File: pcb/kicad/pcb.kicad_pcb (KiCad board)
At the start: 2 copper layers, 56.3 x 62.8 mm, 45 parts, among them J1 Raspberry_Pi_2_3, U1 MCP4822, U2 TL082, U3 TL082, U4 LM358, U5 ADC0831, U6 AOZ1282CI

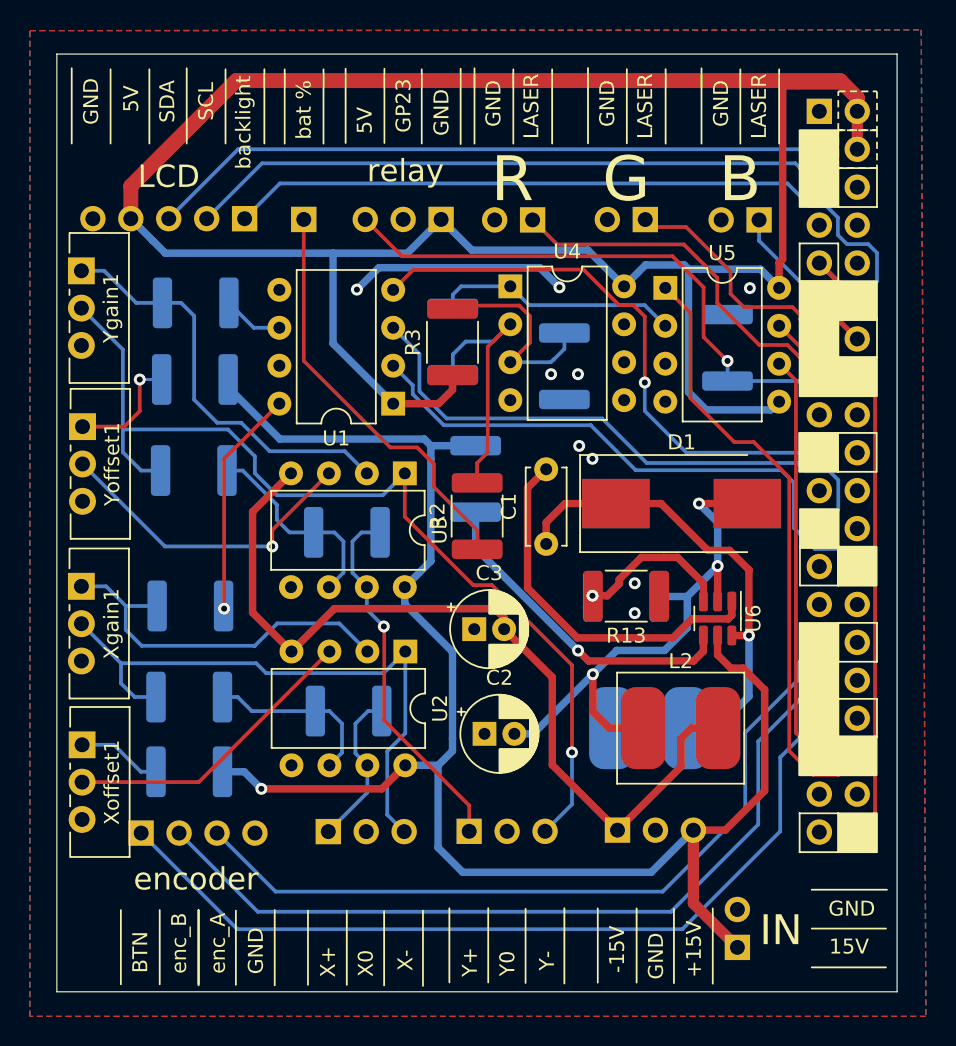
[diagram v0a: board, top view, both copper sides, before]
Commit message: jlc order sent - pcb finished
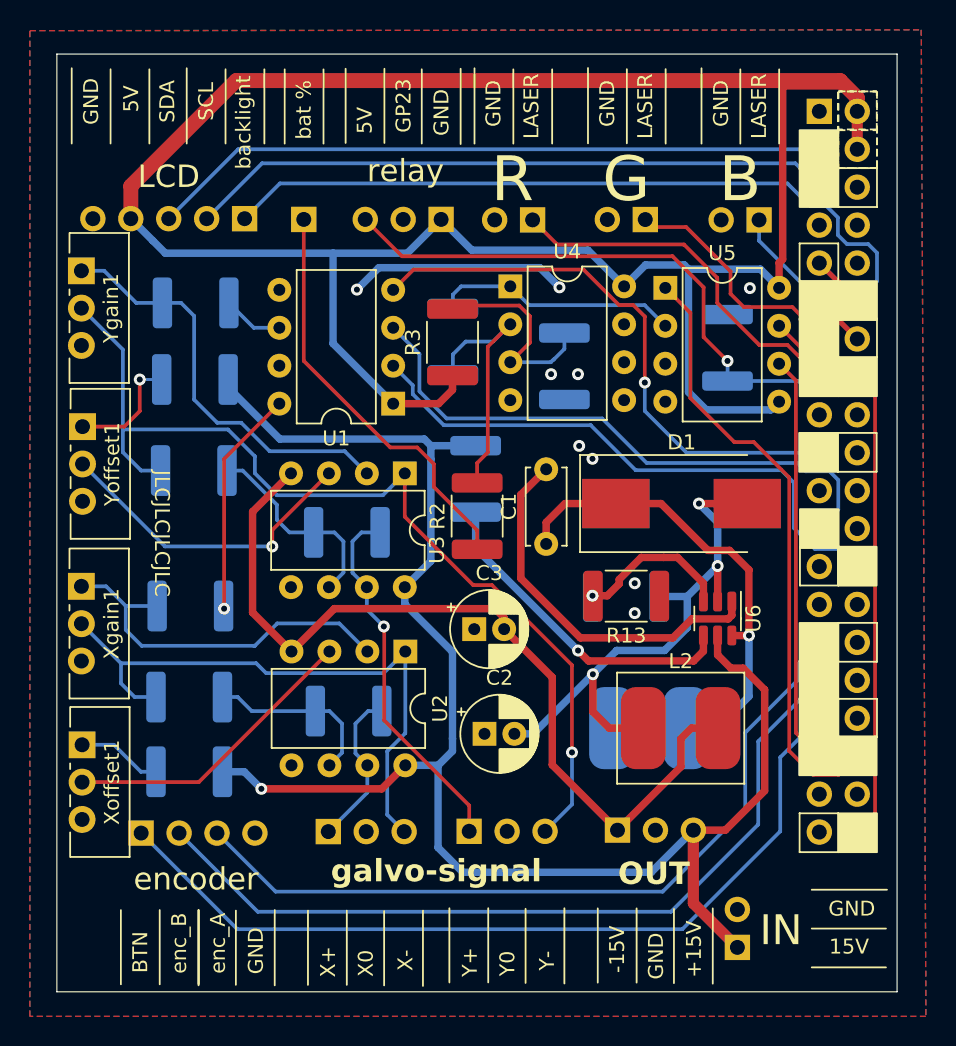
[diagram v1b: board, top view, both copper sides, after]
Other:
- board text added: "JLCJLCJLCJLC"
- board text added: "OUT"
- board text added: "galvo-signal"
